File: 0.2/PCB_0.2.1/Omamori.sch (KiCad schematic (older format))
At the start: 29 parts, among them J1 Conn_01x04_Female, U1 BQ25504, U2 TPS61222DCK, U3 ATtiny85, U4 TS-1233

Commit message: Updated 0.2.1 PCB design.
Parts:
- removed D2: DIODE, Diode_SMD:D_SOD-323_HandSoldering, symbol pspice:DIODE
- added Q1: IRLML0030, Package_TO_SOT_SMD:SOT-23, symbol Transistor_FET:IRLML0030
- added R_oc3: 1.8M, Resistor_SMD:R_0603_1608Metric_Pad0.98x0.95mm_HandSolder, symbol Device:R
- added R_oc4: 8.2M, Resistor_SMD:R_0603_1608Metric_Pad0.98x0.95mm_HandSolder, symbol Device:R
- added R_oc5: 10M, Resistor_SMD:R_0603_1608Metric_Pad0.98x0.95mm_HandSolder, symbol Device:R
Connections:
- net GND: now also R_oc5.1
- net Vbat_ok: now also Q1.1 (G); no longer U2.6 (EN)
- net Vmeasure: now also R_oc3.2, R_oc4.2
- net at C_super1.1, U1.14 (VBAT): now also Q1.3 (D)
- net Vstor: no longer names the net of C_filter1.1, C_pre_boost1.1, L_boost1.1, U2.1 (VIN)
- net Vstor: now also U2.6 (EN), Q1.2 (S), R_oc3.1; no longer U1.15 (VSTOR)
- new net: R_oc4.1, R_oc5.2
- no-connect marks 3 -> 4
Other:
- note added: "5V Boost Converter\n"
- note added: "AT Tiny\n"
- note added: "Photovoltaic"
- note added: "RGBW LED"
- note added: "Serial Pins\n"
- note added: "Solar charge controller"
- note added: "Voltage Divider\n"
- moved on the sheet: C_filter1, C_hvr1, C_led1, C_post_boost1, C_pre_boost1, C_ref1, C_super1, D1, J1, L_boost1, L_bst1, R_data1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

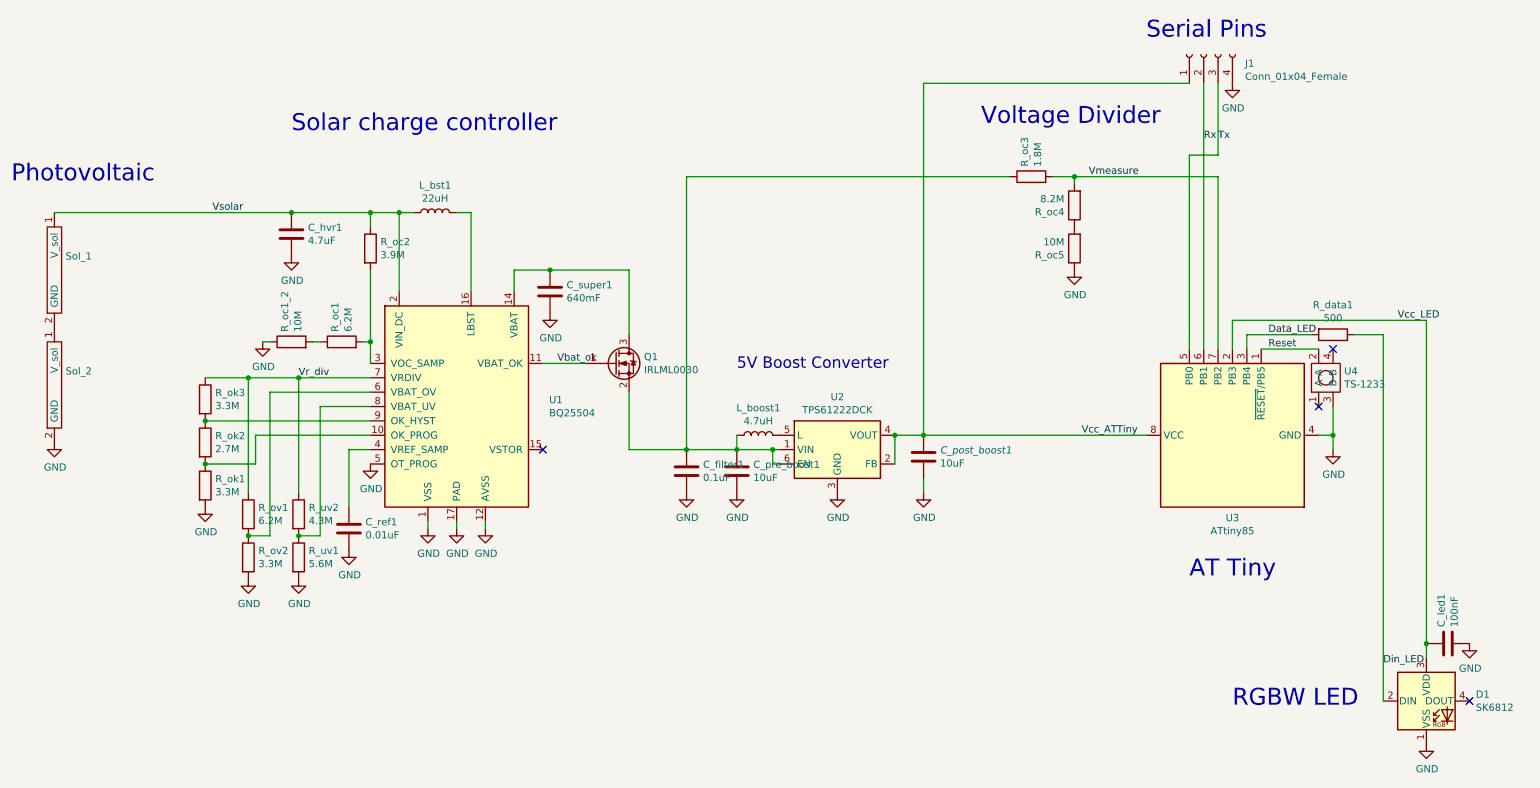
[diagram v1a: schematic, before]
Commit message: Layout and Design redesign.
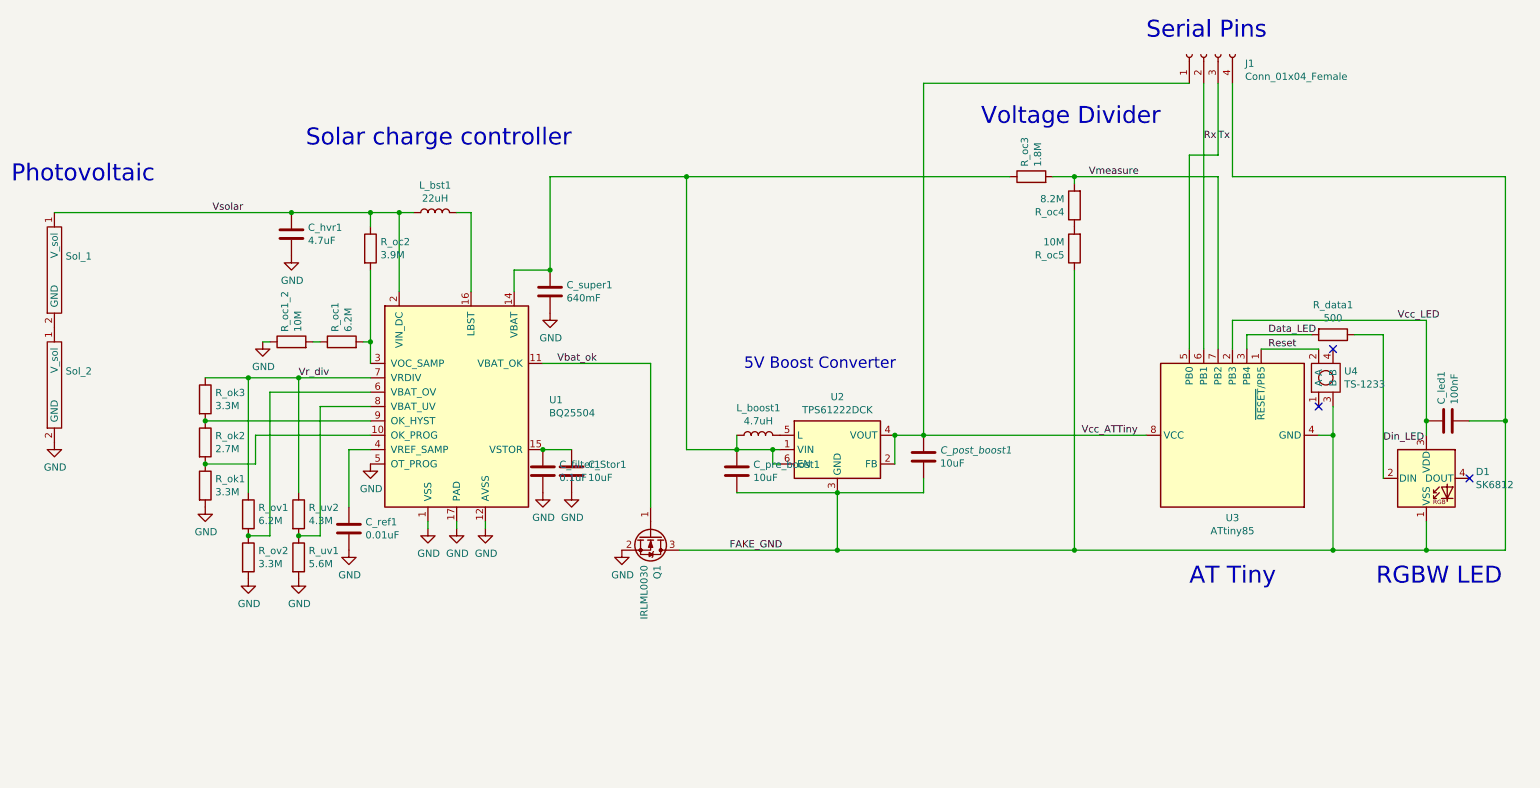
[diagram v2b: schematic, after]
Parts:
- added C_Stor1: 10uF, Capacitor_SMD:C_0805_2012Metric_Pad1.18x1.45mm_HandSolder, symbol Device:C
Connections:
- net GND: now also Q1.2 (S), C_Stor1.2; no longer C_led1.2, C_post_boost1.2, C_pre_boost1.2, D1.1 (VSS), J1.4 (Pin_4), R_oc5.1, U2.3 (GND), U3.4 (GND), U4.3 (B)
- net at C_super1.1, U1.14 (VBAT): now also C_pre_boost1.1, L_boost1.1, R_oc3.1, U2.1 (VIN), U2.6 (EN); no longer Q1.3 (D)
- net at U1.15 (VSTOR): now also C_filter1.1, C_Stor1.1
- new net FAKE_GND: C_led1.2, C_post_boost1.2, C_pre_boost1.2, D1.1 (VSS), J1.4 (Pin_4), Q1.3 (D), R_oc5.1, U2.3 (GND), U3.4 (GND), U4.3 (B)
- no-connect marks 4 -> 3
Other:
- moved on the sheet: C_filter1, C_led1, D1, Q1
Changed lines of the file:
@@
-$EndComp
-$Comp
-L power:GND #PWR018
-U 1 1 60504B03
-P 9750 3700
-F 0 "#PWR018" H 9750 3450 50  0001 C CNN
-F 1 "GND" H 9755 3527 50  0000 C CNN
-F 2 "" H 9750 3700 50  0001 C CNN
-F 3 "" H 9750 3700 50  0001 C CNN
-	1    9750 3700
-	1    0    0    -1
 $EndComp
 $Comp
@@
 	1    0    0    -1
 $EndComp
-$Comp
-L MCU_Microchip_ATtiny:ATtiny13A-SSU U3
-U 1 1 604F4615
-P 9050 3600
-F 0 "U3" V 8475 3600 50  0000 C CNN
-F 1 "ATtiny85" V 8384 3600 50  0000 C CNN
-F 2 "Package_SO:SOIC-8_5.275x5.275mm_P1.27mm" H 9050 3600 50  0001 C CIN
-F 3 "http://ww1.microchip.com/downloads/en/DeviceDoc/doc8126.pdf" H 9050 3600 50  0001 C CNN
-	1    9050 3600
-	0    -1   -1   0
-$EndComp
 Wire Wire Line
 	3250 2050 3250 2600
@@
 Wire Wire Line
 	6700 3600 6900 3600
-$Comp
-L power:GND #PWR015
-U 1 1 609EFD45
-P 6300 4000
-F 0 "#PWR015" H 6300 3750 50  0001 C CNN
-F 1 "GND" H 6305 3827 50  0000 C CNN
-F 2 "" H 6300 4000 50  0001 C CNN
-F 3 "" H 6300 4000 50  0001 C CNN
-	1    6300 4000
-	1    0    0    -1
-$EndComp
 Wire Wire Line
 	6700 3800 6700 3600
@@
 $EndComp
 Connection ~ 6900 3600
-$Comp
-L power:GND #PWR016
-U 1 1 60A26919
-P 6900 4000
-F 0 "#PWR016" H 6900 3750 50  0001 C CNN
-F 1 "GND" H 6905 3827 50  0000 C CNN
-F 2 "" H 6900 4000 50  0001 C CNN
-F 3 "" H 6900 4000 50  0001 C CNN
-	1    6900 4000
-	1    0    0    -1
-$EndComp
 Wire Wire Line
 	6900 4000 6900 3900
@@
 Wire Wire Line
 	9600 2900 9150 2900
-$Comp
-L power:GND #PWR017
-U 1 1 609EA8D2
-P 9050 1150
-F 0 "#PWR017" H 9050 900 50  0001 C CNN
-F 1 "GND" H 9055 977 50  0000 C CNN
-F 2 "" H 9050 1150 50  0001 C CNN
-F 3 "" H 9050 1150 50  0001 C CNN
-	1    9050 1150
-	1    0    0    -1
-$EndComp
 $Comp
 L Connector:Conn_01x04_Female J1
@@
 L power:GND #PWR014
 U 1 1 609F4F40
-P 5250 4000
-F 0 "#PWR014" H 5250 3750 50  0001 C CNN
-F 1 "GND" H 5255 3827 50  0000 C CNN
-F 2 "" H 5250 4000 50  0001 C CNN
-F 3 "" H 5250 4000 50  0001 C CNN
-	1    5250 4000
-	1    0    0    -1
-$EndComp
-$Comp
-L power:GND #PWR013
-U 1 1 60A0DF2C
-P 5600 4000
-F 0 "#PWR013" H 5600 3750 50  0001 C CNN
-F 1 "GND" H 5605 3827 50  0000 C CNN
-F 2 "" H 5600 4000 50  0001 C CNN
-F 3 "" H 5600 4000 50  0001 C CNN
-	1    5600 4000
+P 4250 4000
+F 0 "#PWR014" H 4250 3750 50  0001 C CNN
+F 1 "GND" H 4255 3827 50  0000 C CNN
+F 2 "" H 4250 4000 50  0001 C CNN
+F 3 "" H 4250 4000 50  0001 C CNN
+	1    4250 4000
 	1    0    0    -1
 $EndComp
@@
 L Device:C C_filter1
 U 1 1 609F4440
-P 5250 3850
-F 0 "C_filter1" H 5365 3896 50  0000 L CNN
-F 1 "0.1uF" H 5365 3805 50  0000 L CNN
-F 2 "Capacitor_SMD:C_0603_1608Metric_Pad1.05x0.95mm_HandSolder" H 5288 3700 50  0001 C CNN
-F 3 "~" H 5250 3850 50  0001 C CNN
-	1    5250 3850
+P 4250 3850
+F 0 "C_filter1" H 4365 3896 50  0000 L CNN
+F 1 "0.1uF" H 4365 3805 50  0000 L CNN
+F 2 "Capacitor_SMD:C_0603_1608Metric_Pad1.05x0.95mm_HandSolder" H 4288 3700 50  0001 C CNN
+F 3 "~" H 4250 3850 50  0001 C CNN
+	1    4250 3850
 	1    0    0    -1
 $EndComp
@@
 Text Label 4350 3100 0    50   ~ 0
 Vbat_ok
-$Comp
-L Transistor_FET:IRLML0030 Q1
-U 1 1 61BDECD2
-P 4750 3100
-F 0 "Q1" H 4954 3146 50  0000 L CNN
-F 1 "IRLML0030" H 4954 3055 50  0000 L CNN
-F 2 "Package_TO_SOT_SMD:SOT-23" H 4950 3025 50  0001 L CIN
-F 3 "https://www.infineon.com/dgdl/irlml0030pbf.pdf?fileId=5546d462533600a401535664773825df" H 4750 3100 50  0001 L CNN
-	1    4750 3100
-	1    0    0    -1
-$EndComp
-Wire Wire Line
-	4250 3100 4550 3100
-Wire Wire Line
-	4300 2450 4850 2450
-Wire Wire Line
-	4850 2450 4850 2900
-Connection ~ 4300 2450
-NoConn ~ 4250 3700
-Wire Wire Line
-	4850 3300 4850 3700
 Wire Wire Line
 	5850 3800 5850 3700
@@
 	-1   0    0    1
 $EndComp
-$Comp
-L power:GND #PWR0101
-U 1 1 61C27B5D
-P 7950 2450
-F 0 "#PWR0101" H 7950 2200 50  0001 C CNN
-F 1 "GND" H 7955 2277 50  0000 C CNN
-F 2 "" H 7950 2450 50  0001 C CNN
-F 3 "" H 7950 2450 50  0001 C CNN
-	1    7950 2450
-	1    0    0    -1
-$EndComp
 Wire Wire Line
 	7950 1850 7950 1800
-Wire Wire Line
-	4850 3700 5250 3700
-Connection ~ 5250 3700
 Wire Wire Line
 	6900 3600 8450 3600
@@
 	7950 1800 8950 1800
 Connection ~ 7950 1800
-$Comp
-L LED:SK6812 D1
-U 1 1 604F2786
-P 10400 5450
-F 0 "D1" H 10744 5496 50  0000 L CNN
-F 1 "SK6812" H 10744 5405 50  0000 L CNN
-F 2 "LED_SMD:LED_SK6812_PLCC4_5.0x5.0mm_P3.2mm" H 10450 5150 50  0001 L TNN
-F 3 "https://cdn-shop.adafruit.com/product-files/1138/SK6812+LED+datasheet+.pdf" H 10500 5075 50  0001 L TNN
-	1    10400 5450
-	1    0    0    -1
-$EndComp
-$Comp
-L power:GND #PWR019
-U 1 1 6050B2D5
-P 10400 5750
-F 0 "#PWR019" H 10400 5500 50  0001 C CNN
-F 1 "GND" H 10405 5577 50  0000 C CNN
-F 2 "" H 10400 5750 50  0001 C CNN
-F 3 "" H 10400 5750 50  0001 C CNN
-	1    10400 5750
-	1    0    0    -1
-$EndComp
-NoConn ~ 10700 5450
-Text Label 10100 5200 0    50   ~ 0
-Din_LED
-$Comp
-L Device:C C_led1
-U 1 1 60A4741C
-P 10550 5050
-F 0 "C_led1" H 10665 5096 50  0000 L CNN
-F 1 "100nF" H 10665 5005 50  0000 L CNN
-F 2 "Capacitor_SMD:C_0603_1608Metric_Pad1.05x0.95mm_HandSolder" H 10588 4900 50  0001 C CNN
-F 3 "~" H 10550 5050 50  0001 C CNN
-	1    10550 5050
-	0    -1   -1   0
-$EndComp
-Wire Wire Line
-	10400 5150 10400 5050
-Connection ~ 10400 5050
-$Comp
-L power:GND #PWR020
-U 1 1 60A47EBA
-P 10700 5050
-F 0 "#PWR020" H 10700 4800 50  0001 C CNN
-F 1 "GND" H 10705 4877 50  0000 C CNN
-F 2 "" H 10700 5050 50  0001 C CNN
-F 3 "" H 10700 5050 50  0001 C CNN
-	1    10700 5050
-	1    0    0    -1
-$EndComp
-Wire Wire Line
-	10100 5450 10100 2900
 Wire Wire Line
 	10100 2900 9900 2900
@@
 Connection ~ 9750 3600
 Wire Wire Line
-	9750 3600 9750 3700
-Wire Wire Line
 	9050 2800 10400 2800
-Wire Wire Line
-	10400 2800 10400 5050
-Text Notes 5600 3150 0    79   ~ 0
+Text Notes 5650 3150 0    79   ~ 0
 5V Boost Converter\n
 Text Notes 7300 1450 0    118  ~ 0
@@
 Text Notes 8450 850  0    118  ~ 0
 Serial Pins\n
-Text Notes 8750 4600 0    118  ~ 0
+Text Notes 8750 4650 0    118  ~ 0
 AT Tiny\n
-Text Notes 9050 5500 0    118  ~ 0
+Text Notes 10050 4650 0    118  ~ 0
 RGBW LED
-Text Notes 2500 1500 0    118  ~ 0
+Text Notes 2600 1600 0    118  ~ 0
 Solar charge controller
 Text Notes 550  1850 0    118  ~ 0
 Photovoltaic
+$Comp
+L power:GND #PWR0101
+U 1 1 61C12810
+P 4450 4000
+F 0 "#PWR0101" H 4450 3750 50  0001 C CNN
+F 1 "GND" H 4455 3827 50  0000 C CNN
+F 2 "" H 4450 4000 50  0001 C CNN
+F 3 "" H 4450 4000 50  0001 C CNN
+	1    4450 4000
+	1    0    0    -1
+$EndComp
+$Comp
+L Device:C C_Stor1
+U 1 1 61C12816
+P 4450 3850
+F 0 "C_Stor1" H 4565 3896 50  0000 L CNN
+F 1 "10uF" H 4565 3805 50  0000 L CNN
+F 2 "Capacitor_SMD:C_0805_2012Metric_Pad1.18x1.45mm_HandSolder" H 4488 3700 50  0001 C CNN
+F 3 "~" H 4450 3850 50  0001 C CNN
+	1    4450 3850
+	1    0    0    -1
+$EndComp
+Wire Wire Line
+	4250 3700 4450 3700
+Connection ~ 4250 3700
+Connection ~ 4300 2450
+Wire Wire Line
+	5250 1800 4300 1800
+Wire Wire Line
+	4300 1800 4300 2450
+Connection ~ 5250 1800
+$Comp
+L MCU_Microchip_ATtiny:ATtiny13A-SSU U3
+U 1 1 604F4615
+P 9050 3600
+F 0 "U3" V 8475 3600 50  0000 C CNN
+F 1 "ATtiny85" V 8384 3600 50  0000 C CNN
+F 2 "Package_SO:SOIC-8_5.275x5.275mm_P1.27mm" H 9050 3600 50  0001 C CIN
+F 3 "http://ww1.microchip.com/downloads/en/DeviceDoc/doc8126.pdf" H 9050 3600 50  0001 C CNN
+	1    9050 3600
+	0    -1   -1   0
+$EndComp
+$Comp
+L power:GND #PWR013
+U 1 1 60A0DF2C
+P 4800 4400
+F 0 "#PWR013" H 4800 4150 50  0001 C CNN
+F 1 "GND" H 4805 4227 50  0000 C CNN
+F 2 "" H 4800 4400 50  0001 C CNN
+F 3 "" H 4800 4400 50  0001 C CNN
+	1    4800 4400
+	1    0    0    -1
+$EndComp
+$Comp
+L Transistor_FET:IRLML0030 Q1
+U 1 1 61BDECD2
+P 5000 4300
+F 0 "Q1" H 5204 4346 50  0000 L CNN
+F 1 "IRLML0030" H 5204 4255 50  0000 L CNN
+F 2 "Package_TO_SOT_SMD:SOT-23" H 5200 4225 50  0001 L CIN
+F 3 "https://www.infineon.com/dgdl/irlml0030pbf.pdf?fileId=5546d462533600a401535664773825df" H 5000 4300 50  0001 L CNN
+	1    5000 4300
+	0    1    1    0
+$EndComp
+Wire Wire Line
+	4250 3100 5000 3100
+Wire Wire Line
+	5600 4000 6300 4000
+Wire Wire Line
+	6300 4000 6900 4000
+Connection ~ 6300 4000
+Wire Wire Line
+	6300 4000 6300 4400
+Wire Wire Line
+	7950 2450 7950 4400
+Wire Wire Line
+	7950 4400 6300 4400
+Wire Wire Line
+	9750 4400 7950 4400
+Wire Wire Line
+	9750 3600 9750 4400
+$Comp
+L LED:SK6812 D1
+U 1 1 604F2786
+P 10400 3900
+F 0 "D1" H 10744 3946 50  0000 L CNN
+F 1 "SK6812" H 10744 3855 50  0000 L CNN
+F 2 "LED_SMD:LED_SK6812_PLCC4_5.0x5.0mm_P3.2mm" H 10450 3600 50  0001 L TNN
+F 3 "https://cdn-shop.adafruit.com/product-files/1138/SK6812+LED+datasheet+.pdf" H 10500 3525 50  0001 L TNN
+	1    10400 3900
+	1    0    0    -1
+$EndComp
+NoConn ~ 10700 3900
+Text Label 10100 3650 0    50   ~ 0
+Din_LED
+$Comp
+L Device:C C_led1
+U 1 1 60A4741C
+P 10550 3500
+F 0 "C_led1" H 10665 3546 50  0000 L CNN
+F 1 "100nF" H 10665 3455 50  0000 L CNN
+F 2 "Capacitor_SMD:C_0603_1608Metric_Pad1.05x0.95mm_HandSolder" H 10588 3350 50  0001 C CNN
+F 3 "~" H 10550 3500 50  0001 C CNN
+	1    10550 3500
+	0    -1   -1   0
+$EndComp
+Wire Wire Line
+	10400 3600 10400 3500
+Connection ~ 10400 3500
+Wire Wire Line
+	10700 3500 10950 3500
+Wire Wire Line
+	10100 3900 10100 2900
+Wire Wire Line
+	10400 4200 10400 4400
+Wire Wire Line
+	10400 4400 9750 4400
+Wire Wire Line
+	10400 4400 10950 4400
+Wire Wire Line
+	10950 3500 10950 4400
+Connection ~ 10400 4400
+Connection ~ 9750 4400
+Wire Wire Line
+	10400 2800 10400 3500
+Connection ~ 7950 4400
+Connection ~ 6300 4400
+Wire Wire Line
+	5200 4400 6300 4400
+Wire Wire Line
+	5000 4100 5000 3100
+Text Label 5550 4400 0    50   ~ 0
+FAKE_GND
+Wire Wire Line
+	9050 1150 9050 1800
+Wire Wire Line
+	9050 1800 10950 1800
+Wire Wire Line
+	10950 1800 10950 3500
+Connection ~ 10950 3500
 $EndSCHEMATC

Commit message: Added pull down resistor.
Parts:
- added R_pulldown1: 10M, Resistor_SMD:R_0603_1608Metric_Pad1.05x0.95mm_HandSolder, symbol Device:R
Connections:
- net GND: now also R_pulldown1.1
- net Vbat_ok: now also R_pulldown1.2
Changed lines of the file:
@@
 $EndComp
 Wire Wire Line
-	4250 3100 5000 3100
+	4250 3100 4700 3100
 Wire Wire Line
 	5600 4000 6300 4000
@@
 	10950 1800 10950 3500
 Connection ~ 10950 3500
+$Comp
+L Device:R R_pulldown1
+U 1 1 61C260A2
+P 4700 3300
+F 0 "R_pulldown1" H 4770 3346 50  0000 L CNN
+F 1 "10M" H 4770 3255 50  0000 L CNN
+F 2 "Resistor_SMD:R_0603_1608Metric_Pad1.05x0.95mm_HandSolder" V 4630 3300 50  0001 C CNN
+F 3 "~" H 4700 3300 50  0001 C CNN
+	1    4700 3300
+	-1   0    0    1
+$EndComp
+$Comp
+L power:GND #PWR0102
+U 1 1 61C28559
+P 4700 3450
+F 0 "#PWR0102" H 4700 3200 50  0001 C CNN
+F 1 "GND" H 4705 3277 50  0000 C CNN
+F 2 "" H 4700 3450 50  0001 C CNN
+F 3 "" H 4700 3450 50  0001 C CNN
+	1    4700 3450
+	1    0    0    -1
+$EndComp
+Wire Wire Line
+	4700 3150 4700 3100
+Connection ~ 4700 3100
+Wire Wire Line
+	4700 3100 5000 3100
 $EndSCHEMATC

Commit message: Minor Layout update.
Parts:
- R_oc1: value 6.2M -> 5.6M
- R_oc2: value 3.9M -> 4.3M
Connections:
- net Vbat: now reaches C_pre_boost1.1, C_super1.1, L_boost1.1, R_oc3.1, U1.14 (VBAT), U2.1 (VIN), U2.6 (EN)
- net FAKE_GND renamed Drain
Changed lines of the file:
@@
 P 3050 2300
 F 0 "R_oc2" H 3120 2346 50  0000 L CNN
-F 1 "3.9M" H 3120 2255 50  0000 L CNN
+F 1 "4.3M" H 3120 2255 50  0000 L CNN
 F 2 "Resistor_SMD:R_0603_1608Metric_Pad1.05x0.95mm_HandSolder" V 2980 2300 50  0001 C CNN
 F 3 "~" H 3050 2300 50  0001 C CNN
@@
 U 1 1 6049F0BD
 P 3650 3400
-F 0 "U1" H 4294 3446 50  0000 L CNN
+F 0 "U1" H 3500 4150 50  0000 L CNN
 F 1 "BQ25504" H 4294 3355 50  0000 L CNN
 F 2 "footprints:VQFN-16-1EP_3x3mm_P0.5mm_EP1.8x1.8mm" H 3650 3400 50  0001 C CNN
@@
 P 2850 2950
 F 0 "R_oc1" H 2920 2996 50  0000 L CNN
-F 1 "6.2M" H 2920 2905 50  0000 L CNN
+F 1 "5.6M" H 2920 2905 50  0000 L CNN
 F 2 "Resistor_SMD:R_0603_1608Metric_Pad0.98x0.95mm_HandSolder" V 2780 2950 50  0001 C CNN
 F 3 "~" H 2850 2950 50  0001 C CNN
@@
 U 1 1 609F4440
 P 4250 3850
-F 0 "C_filter1" H 4365 3896 50  0000 L CNN
-F 1 "0.1uF" H 4365 3805 50  0000 L CNN
+F 0 "C_filter1" H 4150 3950 50  0000 L CNN
+F 1 "0.1uF" H 4200 3750 50  0000 L CNN
 F 2 "Capacitor_SMD:C_0603_1608Metric_Pad1.05x0.95mm_HandSolder" H 4288 3700 50  0001 C CNN
 F 3 "~" H 4250 3850 50  0001 C CNN
@@
 U 1 1 61C12816
 P 4450 3850
-F 0 "C_Stor1" H 4565 3896 50  0000 L CNN
-F 1 "10uF" H 4565 3805 50  0000 L CNN
+F 0 "C_Stor1" H 4500 3950 50  0000 L CNN
+F 1 "10uF" H 4450 3750 50  0000 L CNN
 F 2 "Capacitor_SMD:C_0805_2012Metric_Pad1.18x1.45mm_HandSolder" H 4488 3700 50  0001 C CNN
 F 3 "~" H 4450 3850 50  0001 C CNN
@@
 	5000 4100 5000 3100
 Text Label 5550 4400 0    50   ~ 0
-FAKE_GND
+Drain
 Wire Wire Line
 	9050 1150 9050 1800
@@
 Wire Wire Line
 	4700 3100 5000 3100
+Text Label 4550 1800 0    50   ~ 0
+Vbat
 $EndSCHEMATC
